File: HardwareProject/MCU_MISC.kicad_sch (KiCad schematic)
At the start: 64 parts, among them J5 Conn_01x03, J6 Conn_01x03, J7 SMA, J8 SMA, SW1 焊盘, SW2 Push_Button, SW3 Push_Button, SW4 Push_Button, U10 TJA1044GTK/3Z, U22 TMP112xxDRL, U27 CA-IS3762HN, U28 TME-0505S, U4 HPM6P41IPB1, U6 AT24C08C-SSHM-T, U7 TMP112xxDRL, U8 TMP112xxDRL, U9 SIT3088ETK, Y1 24MHz ±10ppm 6pF

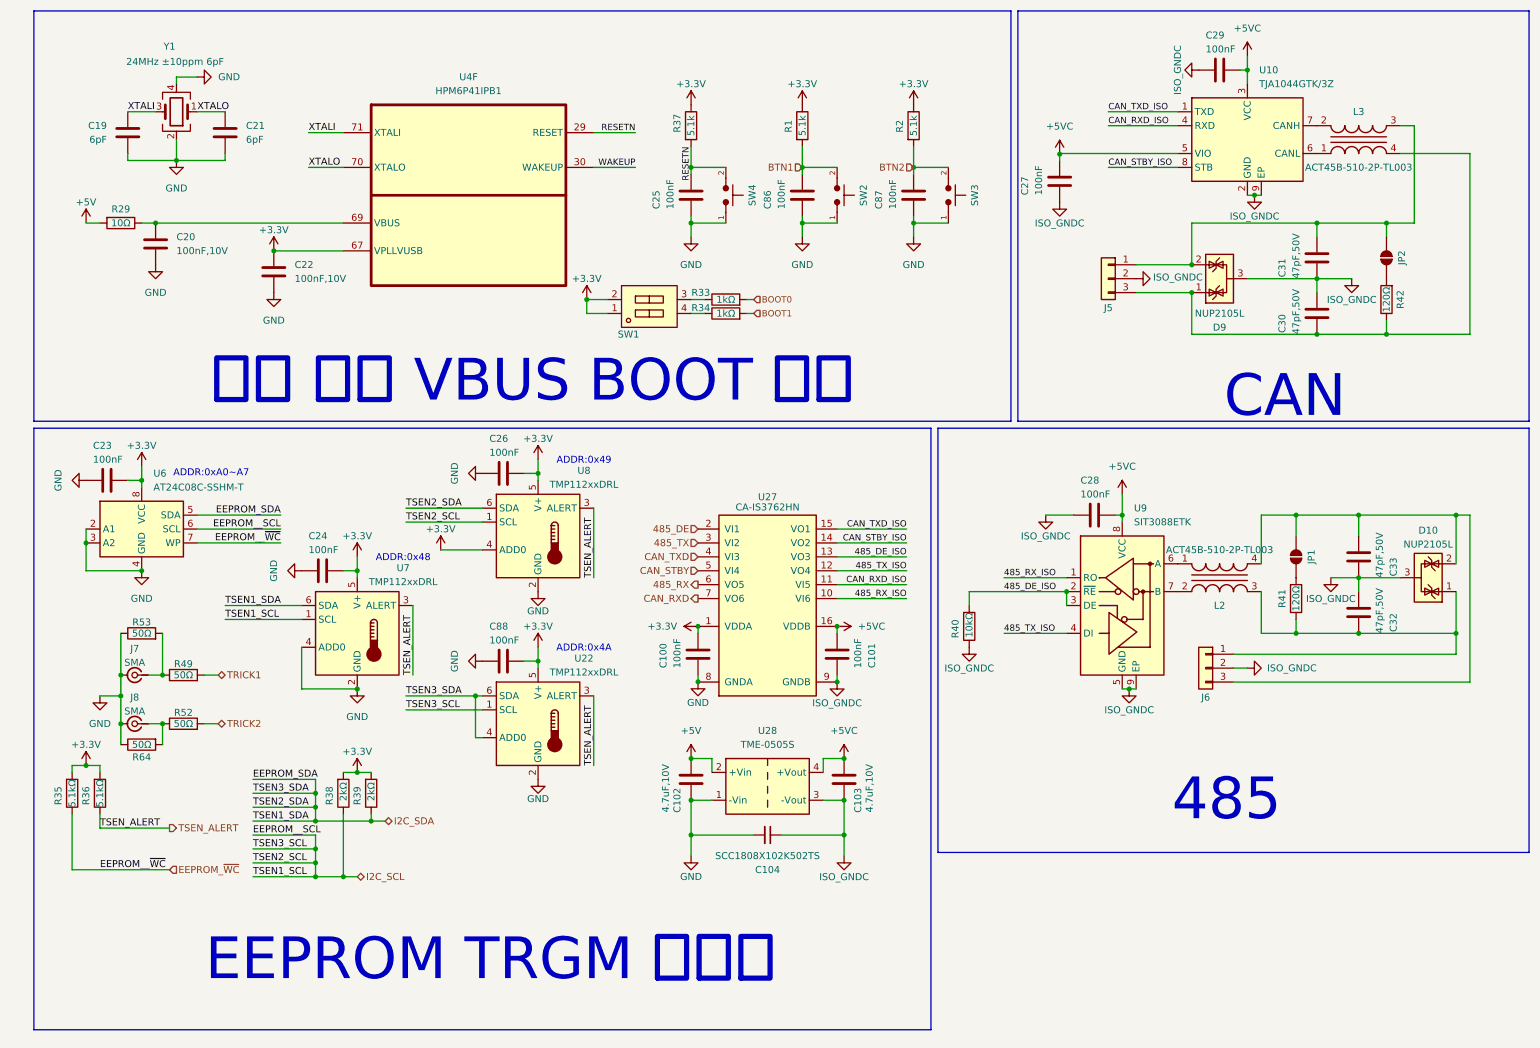
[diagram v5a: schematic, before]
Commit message: rev4修改核心供电前保存（当前SYR838）
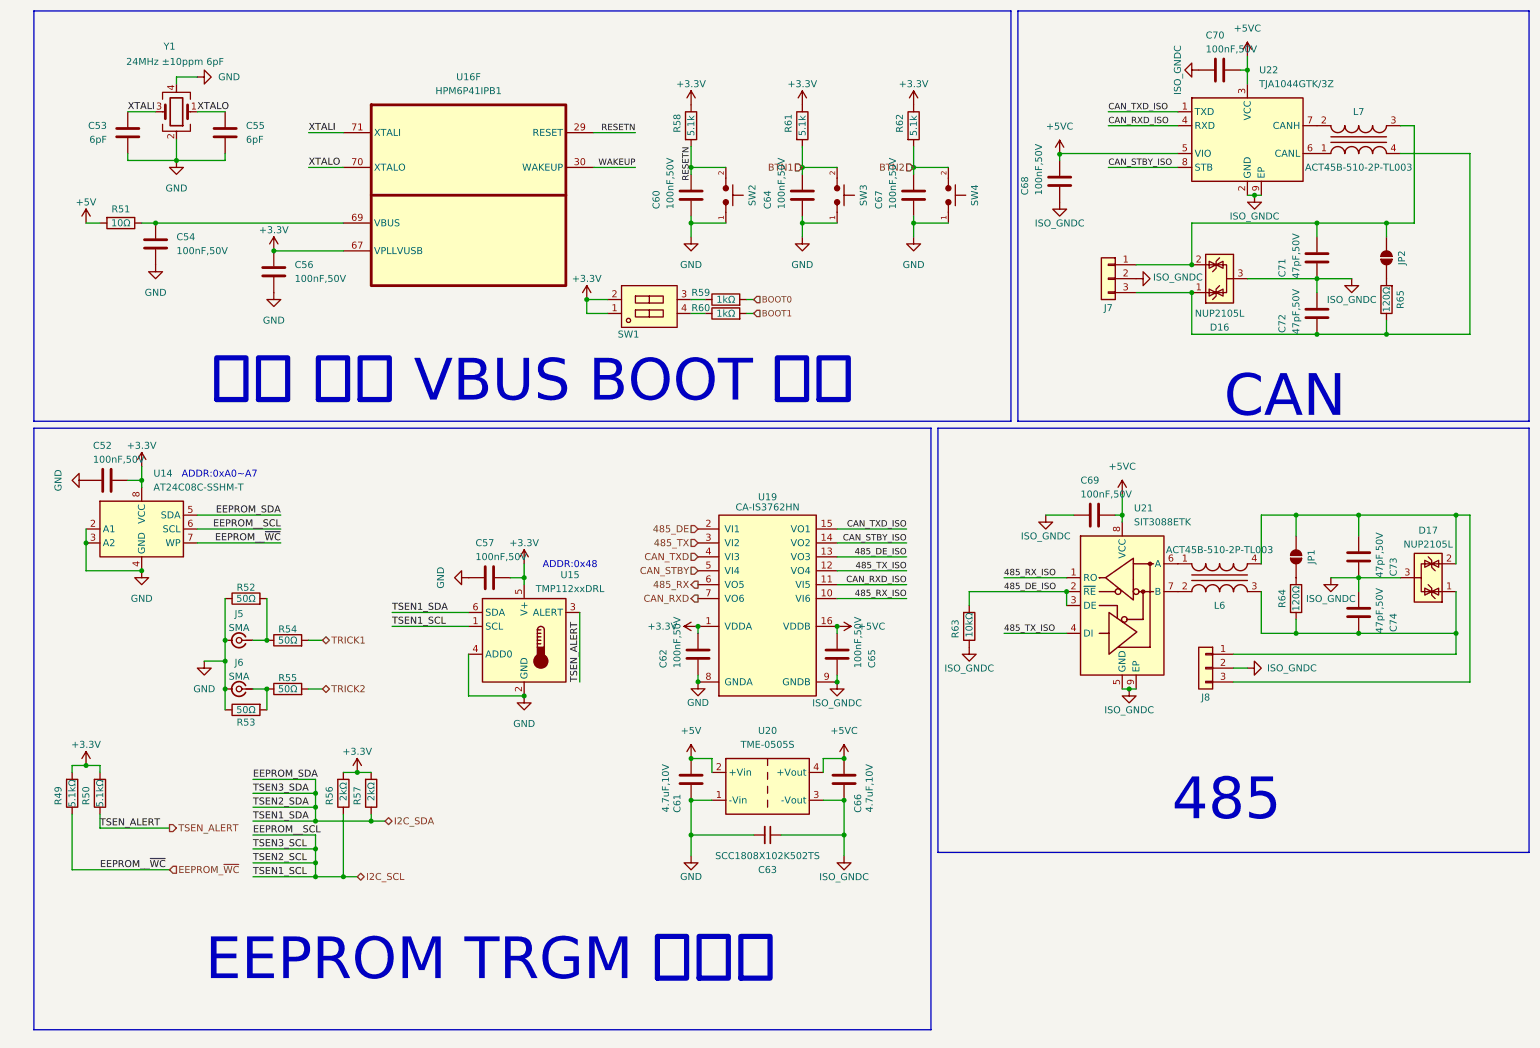
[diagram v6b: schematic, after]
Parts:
- removed C26, C88: 100nF, Capacitor_SMD:C_0603_1608Metric, symbol Device:C
- removed U22, U8: TMP112xxDRL, Package_TO_SOT_SMD:SOT-563, symbol Sensor_Temperature:TMP112xxDRL
- C52: renamed from C23; value 100nF -> 100nF,50V
- C54: renamed from C20; value 100nF,10V -> 100nF,50V
- C56: renamed from C22; value 100nF,10V -> 100nF,50V
- C57: renamed from C24; value 100nF -> 100nF,50V
- C60: renamed from C25; value 100nF -> 100nF,50V
- C62: renamed from C100; value 100nF -> 100nF,50V
- C64: renamed from C86; value 100nF -> 100nF,50V
- C65: renamed from C101; value 100nF -> 100nF,50V
- C67: renamed from C87; value 100nF -> 100nF,50V
- C68: renamed from C27; value 100nF -> 100nF,50V
- C69: renamed from C28; value 100nF -> 100nF,50V
- C70: renamed from C29; value 100nF -> 100nF,50V
- renumbered C19 to C53, C21 to C55, C102 to C61, C104 to C63, C103 to C66, C31 to C71, C30 to C72, C33 to C73, C32 to C74, D9 to D16, D10 to D17, J7 to J5, J8 to J6, J5 to J7, J6 to J8, L2 to L6, L3 to L7, R35 to R49, R36 to R50, R29 to R51, R53 to R52, R64 to R53, R49 to R54, R52 to R55, R38 to R56, R39 to R57, R37 to R58, R33 to R59, R34 to R60, R1 to R61, R2 to R62, R40 to R63, R41 to R64, R42 to R65, SW4 to SW2, SW2 to SW3, SW3 to SW4, U6 to U14, U7 to U15, U4 to U16, U27 to U19, U28 to U20, U9 to U21, U10 to U22
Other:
- note removed: "ADDR:0x49"
- note removed: "ADDR:0x4A"
- moved on the sheet: C57, J5, J6, R52, R53, R54, R55, U15

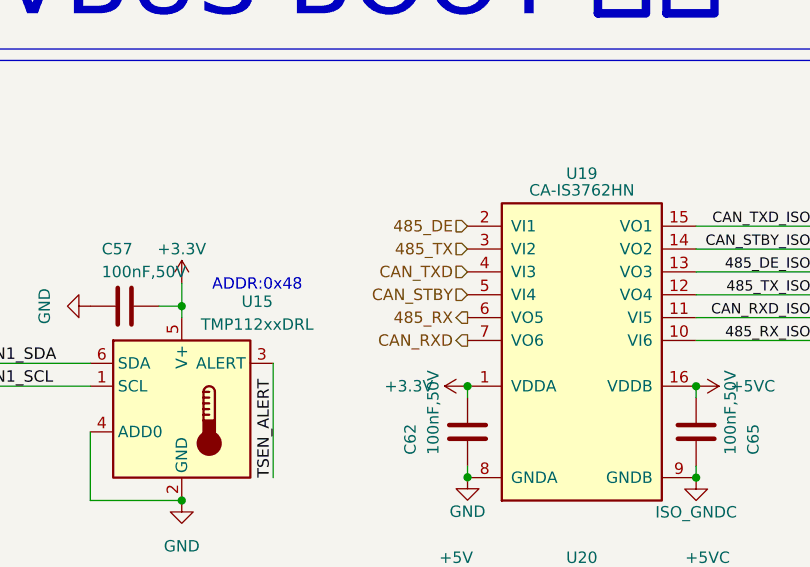
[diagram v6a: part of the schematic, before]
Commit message: 修复：严重BUG！隔离器485与CAN信号完全相反！
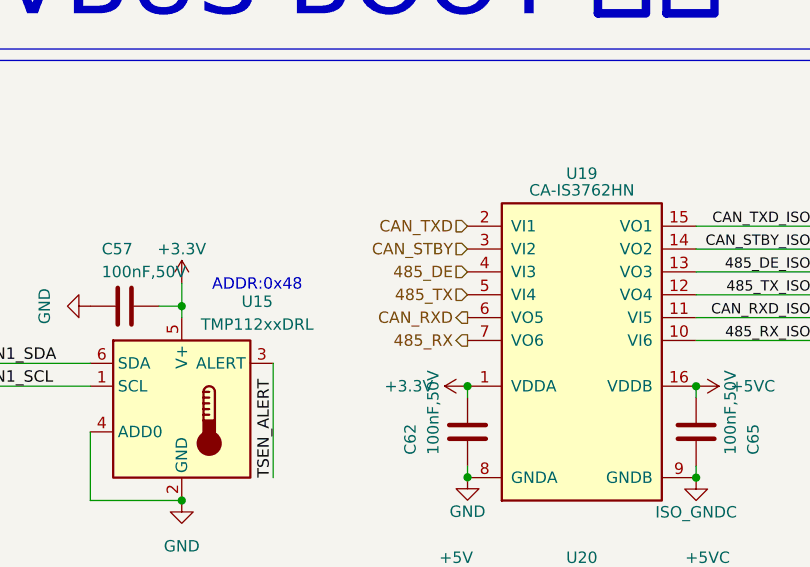
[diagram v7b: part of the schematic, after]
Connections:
- net 485_DE: now also U19.4 (VI3); no longer U19.2 (VI1)
- net 485_RX: now also U19.7 (VO6); no longer U19.6 (VO5)
- net 485_TX: now also U19.5 (VI4); no longer U19.3 (VI2)
- net CAN_RXD: now also U19.6 (VO5); no longer U19.7 (VO6)
- net CAN_STBY: now also U19.3 (VI2); no longer U19.5 (VI4)
- net CAN_TXD: now also U19.2 (VI1); no longer U19.4 (VI3)
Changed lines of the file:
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@@
 	(hierarchical_label "485_RX"
 		(shape output)
-		(at 133.35 116.84 180)
+		(at 133.35 119.38 180)
 		(effects
 			(font
@@
 	(hierarchical_label "CAN_TXD"
 		(shape input)
-		(at 133.35 111.76 180)
+		(at 133.35 106.68 180)
 		(effects
 			(font
@@
 	(hierarchical_label "485_DE"
 		(shape input)
-		(at 133.35 106.68 180)
+		(at 133.35 111.76 180)
 		(effects
 			(font
@@
 	(hierarchical_label "CAN_RXD"
 		(shape output)
-		(at 133.35 119.38 180)
+		(at 133.35 116.84 180)
 		(effects
 			(font
@@
 	(hierarchical_label "485_TX"
 		(shape input)
-		(at 133.35 109.22 180)
+		(at 133.35 114.3 180)
 		(effects
 			(font
@@
 	(hierarchical_label "CAN_STBY"
 		(shape input)
-		(at 133.35 114.3 180)
+		(at 133.35 109.22 180)
 		(effects
 			(font
